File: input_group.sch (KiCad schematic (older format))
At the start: 5 parts, among them U2 74HC245

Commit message: Layout complete
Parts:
- removed C10: 100n, Capacitors_SMD:C_0603_HandSoldering, symbol C_Small
- removed U2: 74HC245, Housings_SOIC:SOIC-20W_7.5x12.8mm_Pitch1.27mm, symbol 74HC245
- added U2: 74HC245_CUSTOM, Housings_SOIC:SOIC-20W_7.5x12.8mm_Pitch1.27mm, symbol 74HC245_CUSTOM
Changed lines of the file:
@@
 $EndComp
 $Comp
-L 74HC245 U2
-U 1 1 5AD30D2C
-P 4550 3000
-AR Path="/5AD2F8CE/5AD30D2C" Ref="U2"  Part="1"
-AR Path="/5AD35DB7/5AD30D2C" Ref="U5"  Part="1"
-F 0 "U2" H 4650 3575 50  0000 L BNN
-F 1 "74HC245" H 4600 2425 50  0000 L TNN
-F 2 "Housings_SOIC:SOIC-20W_7.5x12.8mm_Pitch1.27mm" H 4550 3000 50  0001 C CNN
-F 3 "" H 4550 3000 50  0001 C CNN
-	1    4550 3000
-	1    0    0    -1
-$EndComp
-$Comp
-L VCOM #PWR015
+L VCOM #PWR18
 U 1 1 5AD30D33
 P 3800 1150
-AR Path="/5AD2F8CE/5AD30D33" Ref="#PWR015"  Part="1"
+AR Path="/5AD2F8CE/5AD30D33" Ref="#PWR18"  Part="1"
 AR Path="/5AD35DB7/5AD30D33" Ref="#PWR044"  Part="1"
-F 0 "#PWR015" H 3800 1000 50  0001 C CNN
+F 0 "#PWR18" H 3800 1000 50  0001 C CNN
 F 1 "VCOM" H 3800 1300 50  0000 C CNN
 F 2 "" H 3800 1150 50  0001 C CNN
@@
 $EndComp
 $Comp
-L GND #PWR016
+L GND #PWR19
 U 1 1 5AD30D39
 P 3800 1450
-AR Path="/5AD2F8CE/5AD30D39" Ref="#PWR016"  Part="1"
+AR Path="/5AD2F8CE/5AD30D39" Ref="#PWR19"  Part="1"
 AR Path="/5AD35DB7/5AD30D39" Ref="#PWR045"  Part="1"
-F 0 "#PWR016" H 3800 1200 50  0001 C CNN
+F 0 "#PWR19" H 3800 1200 50  0001 C CNN
 F 1 "GND" H 3800 1300 50  0000 C CNN
 F 2 "" H 3800 1450 50  0001 C CNN
@@
 	3200 3200 3850 3200
 $Comp
-L VDD #PWR017
+L VDD #PWR21
 U 1 1 5AD30DBA
 P 3850 3400
-AR Path="/5AD2F8CE/5AD30DBA" Ref="#PWR017"  Part="1"
+AR Path="/5AD2F8CE/5AD30DBA" Ref="#PWR21"  Part="1"
 AR Path="/5AD35DB7/5AD30DBA" Ref="#PWR046"  Part="1"
-F 0 "#PWR017" H 3850 3250 50  0001 C CNN
+F 0 "#PWR21" H 3850 3250 50  0001 C CNN
 F 1 "VDD" H 3850 3550 50  0000 C CNN
 F 2 "" H 3850 3400 50  0001 C CNN
@@
 $EndComp
 $Comp
-L C_Small C10
-U 1 1 5AD30DD0
-P 4850 1300
-AR Path="/5AD2F8CE/5AD30DD0" Ref="C10"  Part="1"
-AR Path="/5AD35DB7/5AD30DD0" Ref="C29"  Part="1"
-F 0 "C10" H 4860 1370 50  0000 L CNN
-F 1 "100n" H 4860 1220 50  0000 L CNN
-F 2 "Capacitors_SMD:C_0603_HandSoldering" H 4850 1300 50  0001 C CNN
-F 3 "" H 4850 1300 50  0001 C CNN
-	1    4850 1300
-	1    0    0    -1
-$EndComp
-$Comp
-L GND #PWR018
+L GND #PWR20
 U 1 1 5AD30DD7
 P 4550 1600
-AR Path="/5AD2F8CE/5AD30DD7" Ref="#PWR018"  Part="1"
+AR Path="/5AD2F8CE/5AD30DD7" Ref="#PWR20"  Part="1"
 AR Path="/5AD35DB7/5AD30DD7" Ref="#PWR047"  Part="1"
-F 0 "#PWR018" H 4550 1350 50  0001 C CNN
+F 0 "#PWR20" H 4550 1350 50  0001 C CNN
 F 1 "GND" H 4550 1450 50  0000 C CNN
 F 2 "" H 4550 1600 50  0001 C CNN
@@
 	4850 1500 4850 1400
 $Comp
-L VDD #PWR019
+L VDD #PWR17
 U 1 1 5AD30DE2
 P 4550 1000
-AR Path="/5AD2F8CE/5AD30DE2" Ref="#PWR019"  Part="1"
+AR Path="/5AD2F8CE/5AD30DE2" Ref="#PWR17"  Part="1"
 AR Path="/5AD35DB7/5AD30DE2" Ref="#PWR048"  Part="1"
-F 0 "#PWR019" H 4550 850 50  0001 C CNN
+F 0 "#PWR17" H 4550 850 50  0001 C CNN
 F 1 "VDD" H 4550 1150 50  0000 C CNN
 F 2 "" H 4550 1000 50  0001 C CNN
@@
 Wire Wire Line
 	5350 2500 5250 2500
+$Comp
+L 74HC245_CUSTOM U2
+U 1 1 5AD6B6B5
+P 4550 3000
+F 0 "U2" H 4650 3575 50  0000 L BNN
+F 1 "74HC245_CUSTOM" H 4600 2425 50  0000 L TNN
+F 2 "Housings_SOIC:SOIC-20W_7.5x12.8mm_Pitch1.27mm" H 4550 3000 50  0001 C CNN
+F 3 "" H 4550 3000 50  0001 C CNN
+	1    4550 3000
+	1    0    0    -1
+$EndComp
 $EndSCHEMATC

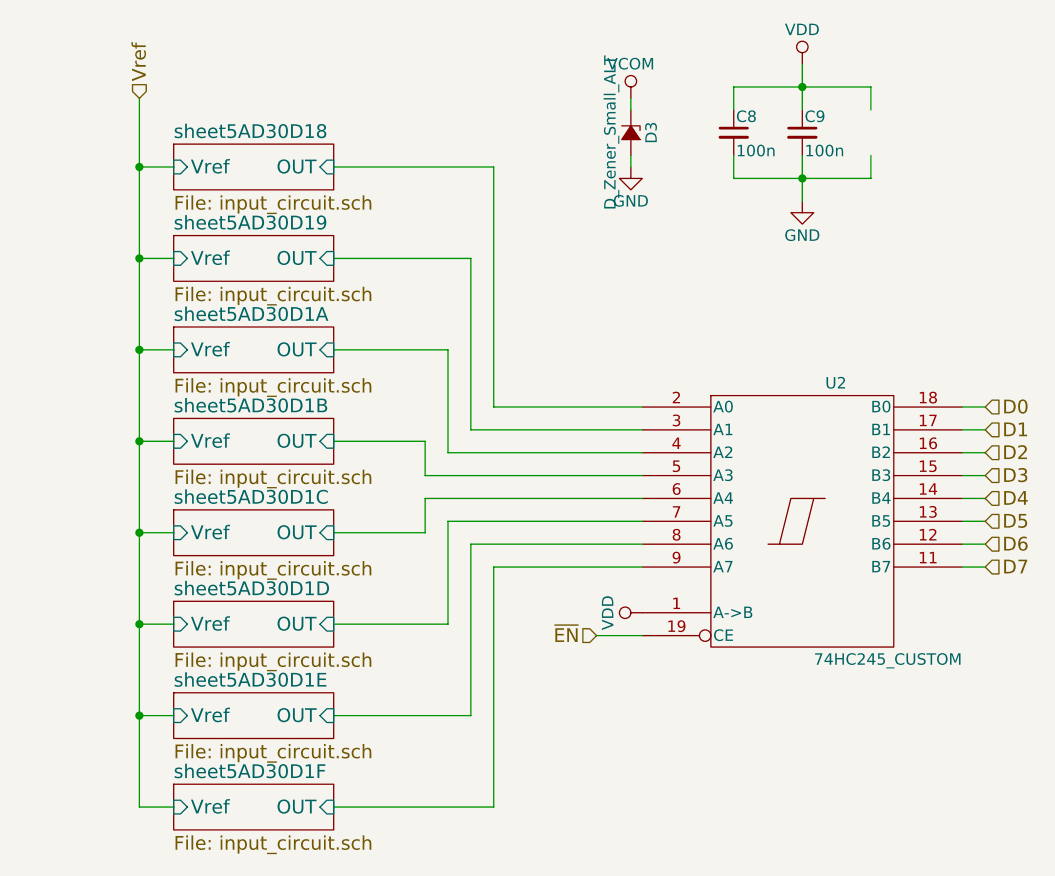
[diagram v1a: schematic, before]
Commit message: Add pullup option
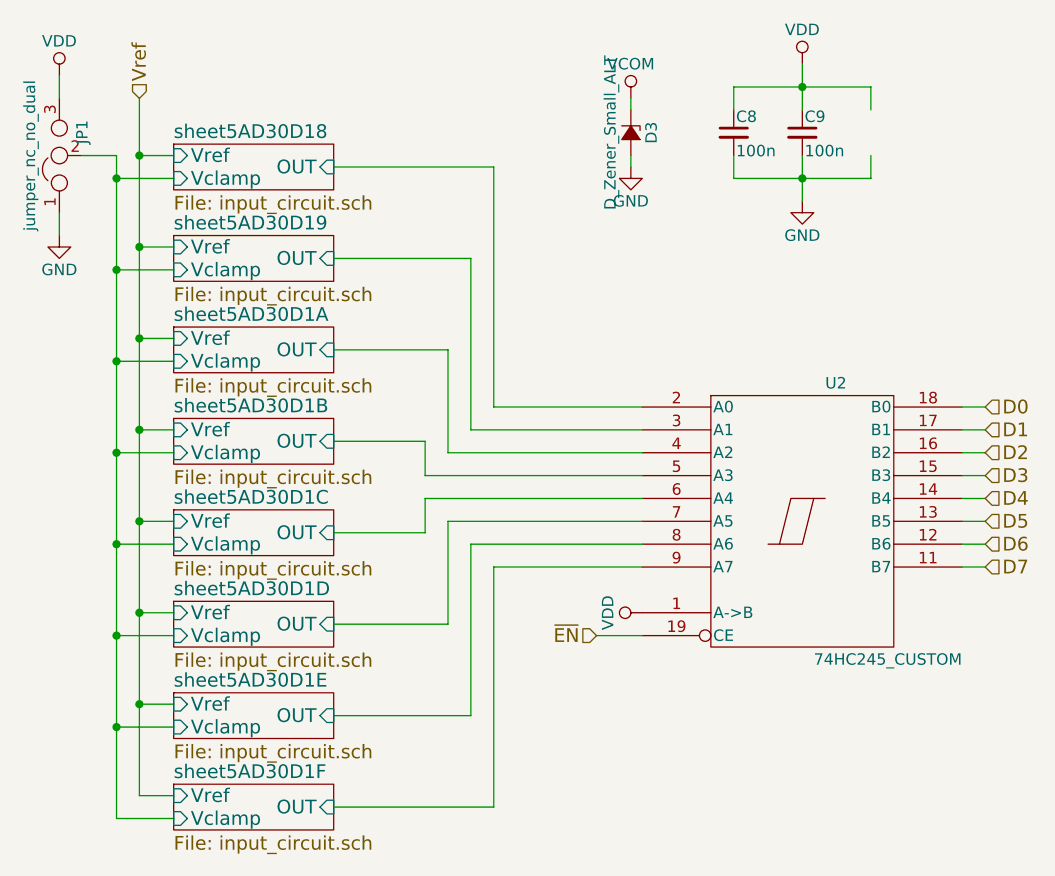
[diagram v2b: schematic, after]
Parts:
- added JP1: jumper_nc_no_dual, footprints:Header_with_SMD_jumper_1x3_2.54, symbol jumper_nc_no_dual
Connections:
- wire segments 52 -> 64
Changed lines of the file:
@@
 $EndComp
 $Comp
-L VCOM #PWR18
+L VCOM #PWR017
 U 1 1 5AD30D33
 P 3800 1150
-AR Path="/5AD2F8CE/5AD30D33" Ref="#PWR18"  Part="1"
+AR Path="/5AD2F8CE/5AD30D33" Ref="#PWR017"  Part="1"
 AR Path="/5AD35DB7/5AD30D33" Ref="#PWR044"  Part="1"
-F 0 "#PWR18" H 3800 1000 50  0001 C CNN
+F 0 "#PWR017" H 3800 1000 50  0001 C CNN
 F 1 "VCOM" H 3800 1300 50  0000 C CNN
 F 2 "" H 3800 1150 50  0001 C CNN
@@
 $EndComp
 $Comp
-L GND #PWR19
+L GND #PWR018
 U 1 1 5AD30D39
 P 3800 1450
-AR Path="/5AD2F8CE/5AD30D39" Ref="#PWR19"  Part="1"
+AR Path="/5AD2F8CE/5AD30D39" Ref="#PWR018"  Part="1"
 AR Path="/5AD35DB7/5AD30D39" Ref="#PWR045"  Part="1"
-F 0 "#PWR19" H 3800 1200 50  0001 C CNN
+F 0 "#PWR018" H 3800 1200 50  0001 C CNN
 F 1 "GND" H 3800 1300 50  0000 C CNN
 F 2 "" H 3800 1450 50  0001 C CNN
@@
 F1 "input_circuit.sch" 60
 F2 "OUT" I R 2500 1450 60
-F3 "Vref" I L 1800 1450 60
+F3 "Vref" I L 1800 1400 60
+F4 "Vclamp" I L 1800 1500 60
 $EndSheet
 $Sheet
@@
 F1 "input_circuit.sch" 60
 F2 "OUT" I R 2500 1850 60
-F3 "Vref" I L 1800 1850 60
+F3 "Vref" I L 1800 1800 60
+F4 "Vclamp" I L 1800 1900 60
 $EndSheet
 $Sheet
@@
 F1 "input_circuit.sch" 60
 F2 "OUT" I R 2500 2250 60
-F3 "Vref" I L 1800 2250 60
+F3 "Vref" I L 1800 2200 60
+F4 "Vclamp" I L 1800 2300 60
 $EndSheet
 $Sheet
@@
 F1 "input_circuit.sch" 60
 F2 "OUT" I R 2500 2650 60
-F3 "Vref" I L 1800 2650 60
+F3 "Vref" I L 1800 2600 60
+F4 "Vclamp" I L 1800 2700 60
 $EndSheet
 $Sheet
@@
 F1 "input_circuit.sch" 60
 F2 "OUT" I R 2500 3050 60
-F3 "Vref" I L 1800 3050 60
+F3 "Vref" I L 1800 3000 60
+F4 "Vclamp" I L 1800 3100 60
 $EndSheet
 $Sheet
@@
 F1 "input_circuit.sch" 60
 F2 "OUT" I R 2500 3450 60
-F3 "Vref" I L 1800 3450 60
-$EndSheet
-$Sheet
-S 1800 3750 700  200
-U 5AD30D7B
-F0 "sheet5AD30D1E" 60
-F1 "input_circuit.sch" 60
-F2 "OUT" I R 2500 3850 60
-F3 "Vref" I L 1800 3850 60
+F3 "Vref" I L 1800 3400 60
+F4 "Vclamp" I L 1800 3500 60
 $EndSheet
 $Sheet
@@
 F1 "input_circuit.sch" 60
 F2 "OUT" I R 2500 4250 60
-F3 "Vref" I L 1800 4250 60
+F3 "Vref" I L 1800 4200 60
+F4 "Vclamp" I L 1800 4300 60
 $EndSheet
 Text HLabel 1650 1150 1    60   Input ~ 0
 Vref
 Wire Wire Line
-	1650 1150 1650 4250
-Wire Wire Line
-	1650 4250 1800 4250
-Wire Wire Line
-	1800 3850 1650 3850
-Connection ~ 1650 3850
-Wire Wire Line
-	1650 3450 1800 3450
-Connection ~ 1650 3450
-Wire Wire Line
-	1800 3050 1650 3050
-Connection ~ 1650 3050
-Wire Wire Line
-	1800 2650 1650 2650
-Connection ~ 1650 2650
-Wire Wire Line
-	1800 2250 1650 2250
-Connection ~ 1650 2250
-Wire Wire Line
-	1800 1850 1650 1850
-Connection ~ 1650 1850
-Wire Wire Line
-	1800 1450 1650 1450
-Connection ~ 1650 1450
+	1650 1150 1650 4200
+Wire Wire Line
+	1650 4200 1800 4200
+Wire Wire Line
+	1800 3800 1650 3800
+Connection ~ 1650 3800
+Wire Wire Line
+	1650 3400 1800 3400
+Connection ~ 1650 3400
+Wire Wire Line
+	1800 3000 1650 3000
+Connection ~ 1650 3000
+Wire Wire Line
+	1800 2600 1650 2600
+Connection ~ 1650 2600
+Wire Wire Line
+	1800 2200 1650 2200
+Connection ~ 1650 2200
+Wire Wire Line
+	1800 1800 1650 1800
+Connection ~ 1650 1800
+Wire Wire Line
+	1800 1400 1650 1400
+Connection ~ 1650 1400
 Wire Wire Line
 	3850 2800 2900 2800
@@
 	3200 3200 3850 3200
 $Comp
-L VDD #PWR21
+L VDD #PWR019
 U 1 1 5AD30DBA
 P 3850 3400
-AR Path="/5AD2F8CE/5AD30DBA" Ref="#PWR21"  Part="1"
+AR Path="/5AD2F8CE/5AD30DBA" Ref="#PWR019"  Part="1"
 AR Path="/5AD35DB7/5AD30DBA" Ref="#PWR046"  Part="1"
-F 0 "#PWR21" H 3850 3250 50  0001 C CNN
+F 0 "#PWR019" H 3850 3250 50  0001 C CNN
 F 1 "VDD" H 3850 3550 50  0000 C CNN
 F 2 "" H 3850 3400 50  0001 C CNN
@@
 $EndComp
 $Comp
-L GND #PWR20
+L GND #PWR020
 U 1 1 5AD30DD7
 P 4550 1600
-AR Path="/5AD2F8CE/5AD30DD7" Ref="#PWR20"  Part="1"
+AR Path="/5AD2F8CE/5AD30DD7" Ref="#PWR020"  Part="1"
 AR Path="/5AD35DB7/5AD30DD7" Ref="#PWR047"  Part="1"
-F 0 "#PWR20" H 4550 1350 50  0001 C CNN
+F 0 "#PWR020" H 4550 1350 50  0001 C CNN
 F 1 "GND" H 4550 1450 50  0000 C CNN
 F 2 "" H 4550 1600 50  0001 C CNN
@@
 	4850 1500 4850 1400
 $Comp
-L VDD #PWR17
+L VDD #PWR021
 U 1 1 5AD30DE2
 P 4550 1000
-AR Path="/5AD2F8CE/5AD30DE2" Ref="#PWR17"  Part="1"
+AR Path="/5AD2F8CE/5AD30DE2" Ref="#PWR021"  Part="1"
 AR Path="/5AD35DB7/5AD30DE2" Ref="#PWR048"  Part="1"
-F 0 "#PWR17" H 4550 850 50  0001 C CNN
+F 0 "#PWR021" H 4550 850 50  0001 C CNN
 F 1 "VDD" H 4550 1150 50  0000 C CNN
 F 2 "" H 4550 1000 50  0001 C CNN
@@
 	1    0    0    -1
 $EndComp
+$Sheet
+S 1800 3750 700  200
+U 5AD30D7B
+F0 "sheet5AD30D1E" 60
+F1 "input_circuit.sch" 60
+F2 "OUT" I R 2500 3850 60
+F3 "Vref" I L 1800 3800 60
+F4 "Vclamp" I L 1800 3900 60
+$EndSheet
+Wire Wire Line
+	1800 4300 1550 4300
+Wire Wire Line
+	1550 4300 1550 1400
+Wire Wire Line
+	1800 1900 1550 1900
+Connection ~ 1550 1900
+Wire Wire Line
+	1800 1500 1550 1500
+Connection ~ 1550 1500
+Wire Wire Line
+	1800 2300 1550 2300
+Connection ~ 1550 2300
+Wire Wire Line
+	1800 2700 1550 2700
+Connection ~ 1550 2700
+Wire Wire Line
+	1550 3100 1800 3100
+Connection ~ 1550 3100
+Wire Wire Line
+	1800 3500 1550 3500
+Connection ~ 1550 3500
+Wire Wire Line
+	1800 3900 1550 3900
+Connection ~ 1550 3900
+$Comp
+L jumper_nc_no_dual JP1
+U 1 1 5AD72B88
+P 1300 1400
+F 0 "JP1" H 1350 1300 50  0000 L CNN
+F 1 "jumper_nc_no_dual" H 1300 1500 50  0000 C BNN
+F 2 "footprints:Header_with_SMD_jumper_1x3_2.54" H 1300 1400 50  0001 C CNN
+F 3 "" H 1300 1400 50  0001 C CNN
+	1    1300 1400
+	0    -1   -1   0
+$EndComp
+Wire Wire Line
+	1550 1400 1400 1400
+$Comp
+L VDD #PWR022
+U 1 1 5AD72E32
+P 1300 1050
+F 0 "#PWR022" H 1300 900 50  0001 C CNN
+F 1 "VDD" H 1300 1200 50  0000 C CNN
+F 2 "" H 1300 1050 50  0001 C CNN
+F 3 "" H 1300 1050 50  0001 C CNN
+	1    1300 1050
+	1    0    0    -1
+$EndComp
+$Comp
+L GND #PWR023
+U 1 1 5AD72EE0
+P 1300 1750
+F 0 "#PWR023" H 1300 1500 50  0001 C CNN
+F 1 "GND" H 1300 1600 50  0000 C CNN
+F 2 "" H 1300 1750 50  0001 C CNN
+F 3 "" H 1300 1750 50  0001 C CNN
+	1    1300 1750
+	1    0    0    -1
+$EndComp
+Wire Wire Line
+	1300 1650 1300 1750
+Wire Wire Line
+	1300 1150 1300 1050
 $EndSCHEMATC

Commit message: 8ch version without buffer
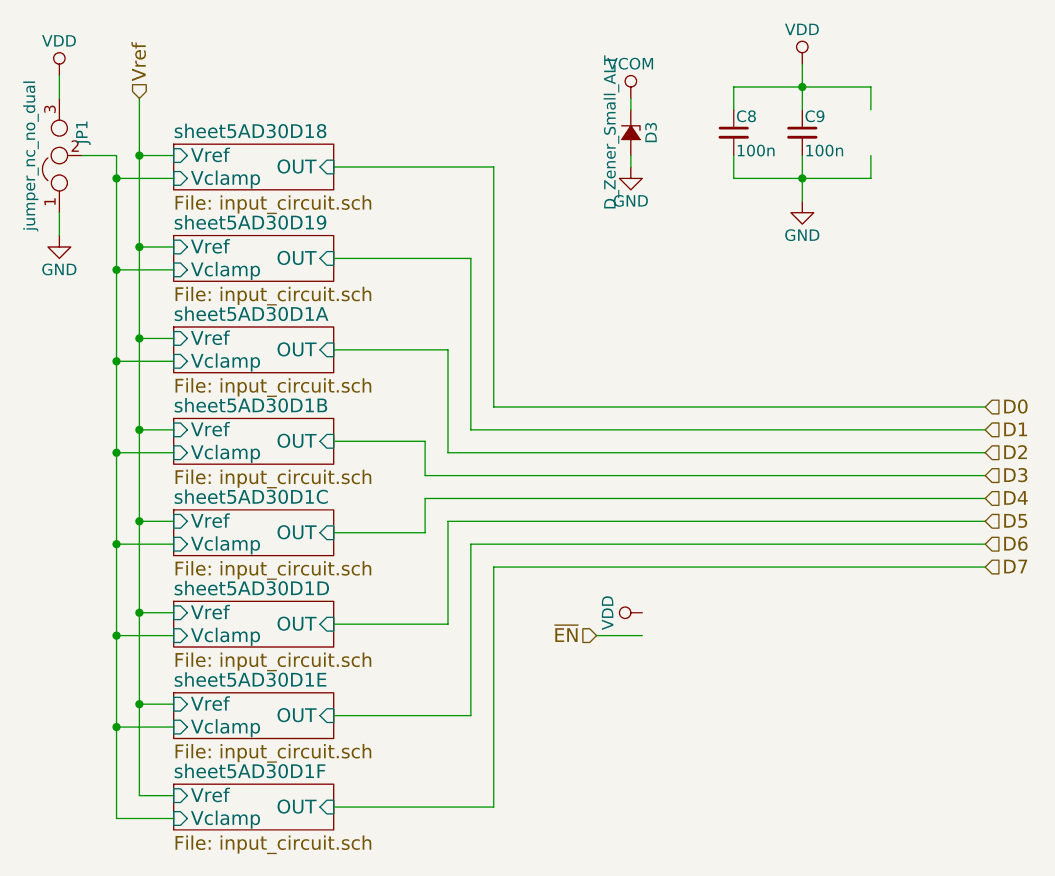
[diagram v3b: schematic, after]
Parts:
- removed U2: 74HC245_CUSTOM, Housings_SOIC:SOIC-20W_7.5x12.8mm_Pitch1.27mm, symbol 74HC245_CUSTOM
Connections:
- wire segments 64 -> 56
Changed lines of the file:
@@
 Connection ~ 1650 1400
 Wire Wire Line
-	3850 2800 2900 2800
+	2900 2800 5350 2800
 Wire Wire Line
 	2900 2800 2900 2650
@@
 	3000 2250 3000 2700
 Wire Wire Line
-	3000 2700 3850 2700
+	3000 2700 5350 2700
 Wire Wire Line
-	3850 2600 3100 2600
+	3100 2600 5350 2600
 Wire Wire Line
 	3100 2600 3100 1850
@@
 	3200 1450 3200 2500
 Wire Wire Line
-	3200 2500 3850 2500
+	3200 2500 5350 2500
 Wire Wire Line
-	3850 2900 2900 2900
+	2900 2900 5350 2900
 Wire Wire Line
 	2900 2900 2900 3050
@@
 	3000 3450 3000 3000
 Wire Wire Line
-	3000 3000 3850 3000
+	3000 3000 5350 3000
 Wire Wire Line
-	3850 3100 3100 3100
+	3100 3100 5350 3100
 Wire Wire Line
 	3100 3100 3100 3850
@@
 	3200 4250 3200 3200
 Wire Wire Line
-	3200 3200 3850 3200
+	3200 3200 5350 3200
 $Comp
 L VDD #PWR019
@@
 Text HLabel 5350 3200 2    60   Input ~ 0
 D7
-Wire Wire Line
-	5350 3200 5250 3200
-Wire Wire Line
-	5350 3100 5250 3100
-Wire Wire Line
-	5250 3000 5350 3000
-Wire Wire Line
-	5350 2900 5250 2900
-Wire Wire Line
-	5250 2800 5350 2800
-Wire Wire Line
-	5350 2700 5250 2700
-Wire Wire Line
-	5250 2600 5350 2600
-Wire Wire Line
-	5350 2500 5250 2500
-$Comp
-L 74HC245_CUSTOM U2
-U 1 1 5AD6B6B5
-P 4550 3000
-F 0 "U2" H 4650 3575 50  0000 L BNN
-F 1 "74HC245_CUSTOM" H 4600 2425 50  0000 L TNN
-F 2 "Housings_SOIC:SOIC-20W_7.5x12.8mm_Pitch1.27mm" H 4550 3000 50  0001 C CNN
-F 3 "" H 4550 3000 50  0001 C CNN
-	1    4550 3000
-	1    0    0    -1
-$EndComp
 $Sheet
 S 1800 3750 700  200
